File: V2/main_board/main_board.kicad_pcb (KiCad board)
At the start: 2 copper layers, 95 x 103.5 mm, 82 parts, among them J1 Conn_01x12, J2 Conn_01x12, J3 OUT_1, J4 OUT_2, J5 EXT_TEMP, J6 USB_C_Receptacle_USB2.0_16P, K1 EE2-3TNUH, Q1 BC817, Q2 BC817, SW1 SW_Slide_DPDT, SW2 SW_Push, SW3 SW_Push, U1 BQ24074RGT, U10 ESP32-S3-WROOM-2, U2 AP7361C-33E, U3 MAX17048G_T10, U4 EL817, U5 EL817, U6 PCF8563T, U8 DS18B20Z, U9 DS18B20Z, Y1 32.768khz

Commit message: In progress
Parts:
- removed C7, C8: 100uF, Capacitor_SMD:CP_Elec_8x10
- removed TP6: IO45, TestPoint:TestPoint_Pad_2.0x2.0mm
- removed TP7: IO46, TestPoint:TestPoint_Pad_2.0x2.0mm
- added K2: Relay_SPST_Latching_2coil, MH_switches:RELAY_G6CK-1117P-US_OMR, F.Cu at (63.0, 96.8)
- added Q3: BC817, Package_TO_SOT_SMD:SOT-23, F.Cu at (-7.70, 109.4)
- added Q4: BC817, Package_TO_SOT_SMD:SOT-23, F.Cu at (-13.5, 109.5)
- added R17: 0R, Resistor_SMD:R_0603_1608Metric, F.Cu at (231.8, 92.1)
- added R18: 120R, Resistor_SMD:R_0603_1608Metric, F.Cu at (-6.50, 94.2)
- added R19: 120R, Resistor_SMD:R_0603_1608Metric, F.Cu at (-14.8, 94.2)
- added U11: EL817, Package_DIP:SMDIP-4_W7.62mm, F.Cu at (-14.8, 101.0)
- added U7: EL817, Package_DIP:SMDIP-4_W7.62mm, F.Cu at (-6.50, 101.0)
- BT5: value RTC_BAT -> CR2032; footprint Battery:BatteryHolder_Keystone_1057_1x2032 -> Battery:BatteryHolder_Keystone_1058_1x2032
- D1: value GREEN -> M7; footprint LED_SMD:LED_0805_2012Metric -> Diode_SMD:D_SMA
- D2: value RED -> M7; footprint LED_SMD:LED_0805_2012Metric -> Diode_SMD:D_SMA
- F1: value 2A -> 10A; footprint Fuse:Fuse_Schurter_UMZ250 -> Fuse:Fuse_Schurter_UMT250; moved to B.Cu
- F2: value 2A -> 10A; footprint Fuse:Fuse_Schurter_UMZ250 -> Fuse:Fuse_Schurter_UMT250
- J1, J2: value Conn_01x12 -> Conn_01x14; footprint Connector_PinHeader_2.54mm:PinHeader_1x12_P2.54mm_Vertical_SMD_Pin1Left -> Connector_PinSocket_2.54mm:PinSocket_1x14_P2.54mm_Vertical_SMD_Pin1Left
- J3, J4: footprint TerminalBlock_Phoenix:TerminalBlock_Phoenix_MKDS-1,5-3_1x03_P5.00mm_Horizontal -> MH_connectors:SAMESKY_TBLH10-508-02BK
- K1: value EE2-3TNUH -> Relay_SPST_Latching_2coil; footprint Relay_SMD:Relay_DPDT_Kemet_EE2_NUH_DoubleCoil -> MH_switches:RELAY_G6CK-1117P-US_OMR
- R8, R9: value 1.5K -> 4.7k
- moved U2 136.7 mm to (-17.8, 71.0), turned to 90 degrees
- moved C4 129.8 mm to (-20.0, 77.5), turned to -90 degrees
- moved C5 126.9 mm to (-15.2, 77.5), turned to -90 degrees
- moved U5 117.2 mm to (-23.0, 101.1), turned to -90 degrees
- moved Q2 115.3 mm to (-24.2, 109.5), turned to -90 degrees
- moved Q1 115.3 mm to (-29.7, 109.5), turned to -90 degrees
- moved R11 114.2 mm to (-23.0, 94.3), turned to 0 degrees
- moved U4 111.7 mm to (-31.0, 101.1), turned to -90 degrees
- moved D6 110.0 mm to (217.5, 86.8), turned to 180 degrees
- moved R10 109.0 mm to (-31.2, 94.3), turned to 0 degrees
- moved BT5 107.6 mm to (221.2, 63.8)
- moved R12 106.6 mm to (220.5, 84.1), turned to 180 degrees
- moved C9 106.2 mm to (221.5, 92.3), turned to 180 degrees
- moved Y1 106.2 mm to (226.5, 92.3)
- moved J6 105.8 mm to (53.4, 69.6), turned to -90 degrees
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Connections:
- net /RELAY_RESET renamed /RELAY1_RESET
- net /RELAY_SET renamed /RELAY1_SET
- D1 pad 1: Net-(D1-K) -> +3V3
- D2 pad 1: Net-(D2-K) -> +3V3
- D5 pad 2: +3V3 -> Net-(D5-A)
- F1 pad 1: Net-(F1-Pad1) -> Net-(J3-Pin_1)
- F1 pad 2: Net-(J4-Pin_2) -> Net-(F1-Pad2)
- F2 pad 1: Net-(F2-Pad1) -> Net-(J4-Pin_1)
- F2 pad 2: Net-(J3-Pin_2) -> Net-(F2-Pad2)
- J1 pad 11: /LED_PWM -> GND
- J1 pad 12: GND -> /PGOOD
- R8 pad 1: VPP -> +3V3
- R8 pad 2: Net-(D1-K) -> /I2C_SDA
- R9 pad 1: Net-(D2-K) -> +3V3
- R9 pad 2: VPP -> /I2C_SCL
- U1 pad 7: Net-(D1-A) -> /PGOOD
- U1 pad 9: Net-(D2-A) -> /CHG
- U10 pad 16: Net-(U10-IO46) -> /RELAY2_RESET
- U10 pad 26: Net-(U10-IO45) -> /RELAY2_SET
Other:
- board size 95 x 103.5 mm -> 141.7 x 103.5 mm

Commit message: in progress
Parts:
- F1: moved to F.Cu
- moved K1 22.0 mm to (52.0, 141.2), turned to -90 degrees
- moved F1 18.3 mm to (67.2, 109.0)
- moved BT1 15.7 mm to (110.5, 69.2)
- moved SW1 15.1 mm to (153.8, 74.2)
- moved K2 11.7 mm to (51.6, 99.1), turned to -90 degrees
- moved J4 8.75 mm to (57.2, 121.8)
- moved BT4 8.49 mm to (110.8, 133.9)
- moved BT2 8.42 mm to (110.5, 90.6)
- moved BT3 7.96 mm to (110.6, 112.1)
- moved J3 7.29 mm to (57.2, 110.5)
- moved H2 6.67 mm to (145.5, 54.5)
- moved H4 6.67 mm to (145.5, 149.0), turned to 90 degrees
- moved F2 5.30 mm to (67.2, 121.8)
- moved H1 2.12 mm to (54.5, 54.5)
- moved H3 2.12 mm to (54.5, 149.0), turned to -90 degrees
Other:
- board size 141.7 x 103.5 mm -> 100 x 103.5 mm

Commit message: Push progress
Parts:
- removed J2: Conn_01x14, Connector_PinSocket_2.54mm:PinSocket_1x14_P2.54mm_Vertical_SMD_Pin1Left
- D1, D2, D3, D4: moved to B.Cu
- J1: value Conn_01x14 -> Conn_02x14_Top_Bottom; footprint Connector_PinSocket_2.54mm:PinSocket_1x14_P2.54mm_Vertical_SMD_Pin1Left -> Connector_PinHeader_2.54mm:PinHeader_2x14_P2.54mm_Vertical_SMD
- moved J5 147.4 mm to (51.2, 68.0), turned to -90 degrees
- moved R17 146.4 mm to (89.5, 57.5), turned to 90 degrees
- moved D5 144.2 mm to (89.5, 63.0), turned to 90 degrees
- moved Y1 136.3 mm to (94.8, 57.2), turned to 180 degrees
- moved TP3 136.1 mm to (92.8, 69.8), turned to 180 degrees
- moved U6 131.9 mm to (95.8, 63.0), turned to -90 degrees
- moved C9 126.7 mm to (99.8, 57.2), turned to 0 degrees
- moved R10 121.2 mm to (90.0, 98.5), turned to -90 degrees
- moved R12 121.2 mm to (100.8, 65.5), turned to 0 degrees
- moved D6 119.0 mm to (99.8, 69.5), turned to 0 degrees
- moved U4 114.5 mm to (83.5, 98.5), turned to 180 degrees
- moved R11 114.1 mm to (90.0, 110.5), turned to -90 degrees
- moved J6 112.1 mm to (131.7, 149.9), turned to 0 degrees
- moved C4 110.0 mm to (89.5, 87.9)
- moved C5 110.0 mm to (94.3, 87.8)
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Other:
- outline, holes or cut-outs redrawn

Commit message: Start layout
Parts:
- removed J4: OUT_2, MH_connectors:SAMESKY_TBLH10-508-02BK
- added J2: OUT_1, MH_connectors:CONN2_2604-1102_WAG, B.Cu at (60.5, 69.4)
- F1, F2: footprint Fuse:Fuse_Schurter_UMT250 -> Fuse:Fuseholder_Clip-5x20mm_Littelfuse_111_Lateral_P18.80x5.00mm_D1.17mm_Horizontal; moved to B.Cu
- J3: value OUT_1 -> OUT_2; footprint MH_connectors:SAMESKY_TBLH10-508-02BK -> MH_connectors:CONN2_2604-1102_WAG; moved to B.Cu
- moved C4 89.8 mm to (178.2, 74.0)
- moved C5 89.8 mm to (183.0, 74.0)
- moved U2 89.8 mm to (180.5, 67.5)
- moved J6 78.3 mm to (54.0, 140.0), turned to -90 degrees
- moved BT5 72.6 mm to (186.5, 32.5)
- moved C9 72.6 mm to (165.2, 26.0)
- moved D5 72.6 mm to (155.0, 31.8)
- moved D6 72.6 mm to (165.2, 38.2)
- moved R12 72.6 mm to (166.2, 34.2)
- moved R17 72.6 mm to (155.0, 26.2)
- moved TP3 72.6 mm to (158.2, 38.5)
- moved U6 72.6 mm to (161.2, 31.8)
- moved Y1 72.6 mm to (160.2, 26.0)
- moved R16 68.5 mm to (65.0, 141.0), turned to 0 degrees
- moved R15 65.5 mm to (65.0, 138.0), turned to 0 degrees
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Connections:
- F1 pad 1: Net-(J3-Pin_1) -> Net-(J2-Pin_2)
- F2 pad 1: Net-(J4-Pin_1) -> Net-(J3-Pin_2)
- K1 pad 14: Net-(J4-Pin_2) -> Net-(J3-Pin_1)
- K2 pad 14: Net-(J3-Pin_2) -> Net-(J2-Pin_1)
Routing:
- added copper zone on B.Cu, net Net-(F1-Pad2)
- added copper zone on F.Cu, net Net-(F1-Pad2)
- added copper zone on B.Cu, net Net-(F2-Pad2)
- added copper zone on F.Cu, net Net-(F2-Pad2)
- added copper zone on B.Cu, net Net-(J2-Pin_1)
- added copper zone on F.Cu, net Net-(J2-Pin_1)
- added copper zone on B.Cu, net Net-(J2-Pin_2)
- added copper zone on F.Cu, net Net-(J2-Pin_2)
- added copper zone on B.Cu, net Net-(J3-Pin_1)
- added copper zone on F.Cu, net Net-(J3-Pin_1)
- added copper zone on B.Cu, net Net-(J3-Pin_2)
- added copper zone on F.Cu, net Net-(J3-Pin_2)
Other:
- outline, holes or cut-outs redrawn

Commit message: Routing progress
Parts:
- H1, H2, H3, H4: footprint MountingHole:MountingHole_3.2mm_M3_ISO7380_Pad_TopBottom -> MountingHole:MountingHole_3.2mm_M3_ISO7380
- U11, U4, U5, U7: value EL817 -> LTV-217; footprint Package_DIP:SMDIP-4_W7.62mm -> Package_SO:SOP-4_4.4x2.6mm_P1.27mm
- moved TH1 90.8 mm to (134.4, 57.8), turned to 180 degrees
- moved C5 85.9 mm to (123.0, 135.5), turned to 180 degrees
- moved U2 83.0 mm to (129.5, 133.0), turned to 0 degrees
- moved Y1 81.2 mm to (118.0, 95.4), turned to -90 degrees
- moved C9 79.4 mm to (119.5, 90.9)
- moved C4 79.2 mm to (123.0, 130.8), turned to 180 degrees
- moved U6 74.5 mm to (123.8, 96.2), turned to 0 degrees
- moved BT5 73.3 mm to (124.2, 71.2), turned to 90 degrees
- moved R17 71.6 mm to (123.8, 90.7)
- moved R12 70.5 mm to (129.5, 94.4)
- moved D5 64.2 mm to (129.5, 90.7), turned to 180 degrees
- moved TP3 62.7 mm to (133.8, 96.2)
- moved D6 58.6 mm to (135.5, 88.8), turned to 90 degrees
- moved TP8 40.9 mm to (137.2, 126.5)
- moved R8 34.4 mm to (79.0, 141.8)
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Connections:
- J1 pad 10: /ADDR_LED -> /DISP_SCLK
- J1 pad 11: GND -> /BTN2
- J1 pad 12: /PGOOD -> /DISP_SDA
- J1 pad 13: /CHG -> /BTN3
- J1 pad 14: GND -> /ONEWIRE
- J1 pad 15: /DISP_BUSY -> /BTN4
- J1 pad 16: /DISP_RES -> /TS_INT
- J1 pad 17: /DISP_D/C -> /PRESENCE_RX
- J1 pad 18: /DISP_CS -> /TS_RST
- J1 pad 19: /DISP_SCLK -> /PRESENCE_TX
- J1 pad 2: +3V3 -> /DISP_BUSY
- J1 pad 20: /DISP_SDA -> unconnected-(J1-Pin_20-Pad20)
- J1 pad 21: /ONEWIRE -> /ADDR_LED
- J1 pad 22: /TS_INT -> GND
- J1 pad 23: /TS_RST -> GND
- J1 pad 24: /PRESENCE_TX -> /PGOOD
- J1 pad 25: /PRESENCE_RX -> /LED_PWM
- J1 pad 26: GND -> /CHG
- J1 pad 27: /LED_PWM -> GND
- J1 pad 3: /BTN1 -> +3V3
- J1 pad 4: /BTN2 -> /DISP_RES
- J1 pad 5: /BTN3 -> /I2C_SDA
- J1 pad 6: /BTN4 -> /DISP_D/C
- J1 pad 7: /SDA -> /I2C_SCL
- J1 pad 8: /SCL -> /DISP_CS
- J1 pad 9: /LED_G -> /BTN1
- U10 pad 16: /RELAY2_RESET -> unconnected-(U10-IO46-Pad16)
- U10 pad 22: /SCL -> unconnected-(U10-IO14-Pad22)
- U10 pad 23: /RTC_INT -> /RELAY1_SET
- U10 pad 24: /BTN3 -> /RELAY1_RESET
- U10 pad 25: /BTN4 -> /RELAY2_RESET
- U10 pad 32: /LED_G -> /BTN4
- U10 pad 33: /LED_PWM -> /BTN3
- U10 pad 34: /BTN1 -> /BTN2
- U10 pad 35: /BTN2 -> /BTN1
- U10 pad 5: /RELAY1_SET -> /RTC_INT
- U10 pad 6: /RELAY1_RESET -> unconnected-(U10-IO6-Pad6)
- U10 pad 8: /SDA -> unconnected-(U10-IO15-Pad8)
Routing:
- net /ONEWIRE: track 0.00 -> 139.1 mm, vias 0 -> 5
- net +BATT: track 0.00 -> 117.9 mm
- net /I2C_SDA: track 0.00 -> 84.6 mm, vias 0 -> 2
- net /I2C_SCL: track 0.00 -> 77.6 mm, vias 0 -> 2
- net /D+: track 0.00 -> 68.5 mm, vias 0 -> 4
- net /D-: track 0.00 -> 67.4 mm, vias 0 -> 2
- net /BTN1: track 0.00 -> 61.5 mm, vias 0 -> 2
- net /BTN2: track 0.00 -> 56.8 mm, vias 0 -> 2
- net /PRESENCE_RX: track 0.00 -> 55.7 mm, vias 0 -> 2
- net /PRESENCE_TX: track 0.00 -> 53.8 mm, vias 0 -> 2
- net /RELAY1_SET: track 0.00 -> 52.9 mm
- net /BTN3: track 0.00 -> 51.2 mm, vias 0 -> 2
- net /BTN4: track 0.00 -> 46.5 mm, vias 0 -> 2
- net /RELAY1_RESET: track 0.00 -> 43.6 mm
- net /VBUS_SW: track 0.00 -> 29.6 mm
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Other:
- outline, holes or cut-outs redrawn
- copper layers 2 -> 4

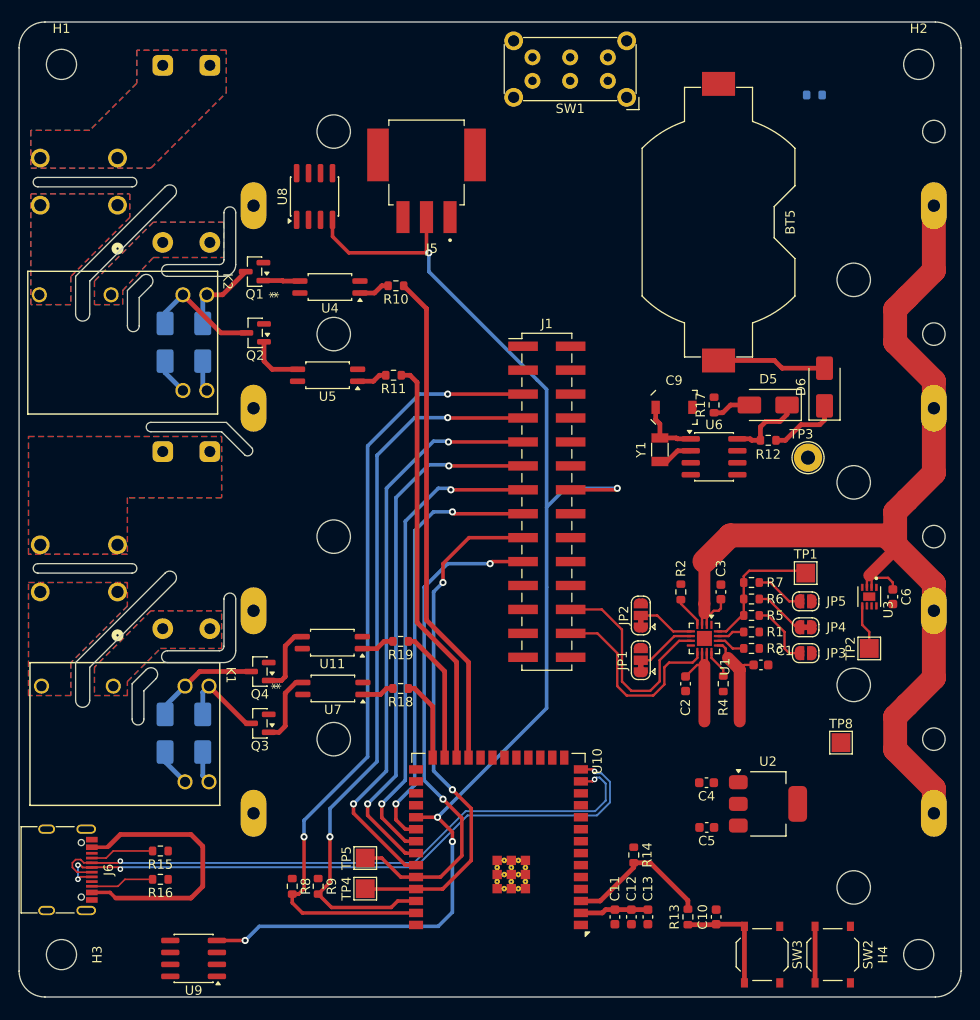
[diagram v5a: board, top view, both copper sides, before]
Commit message: Schematic updates
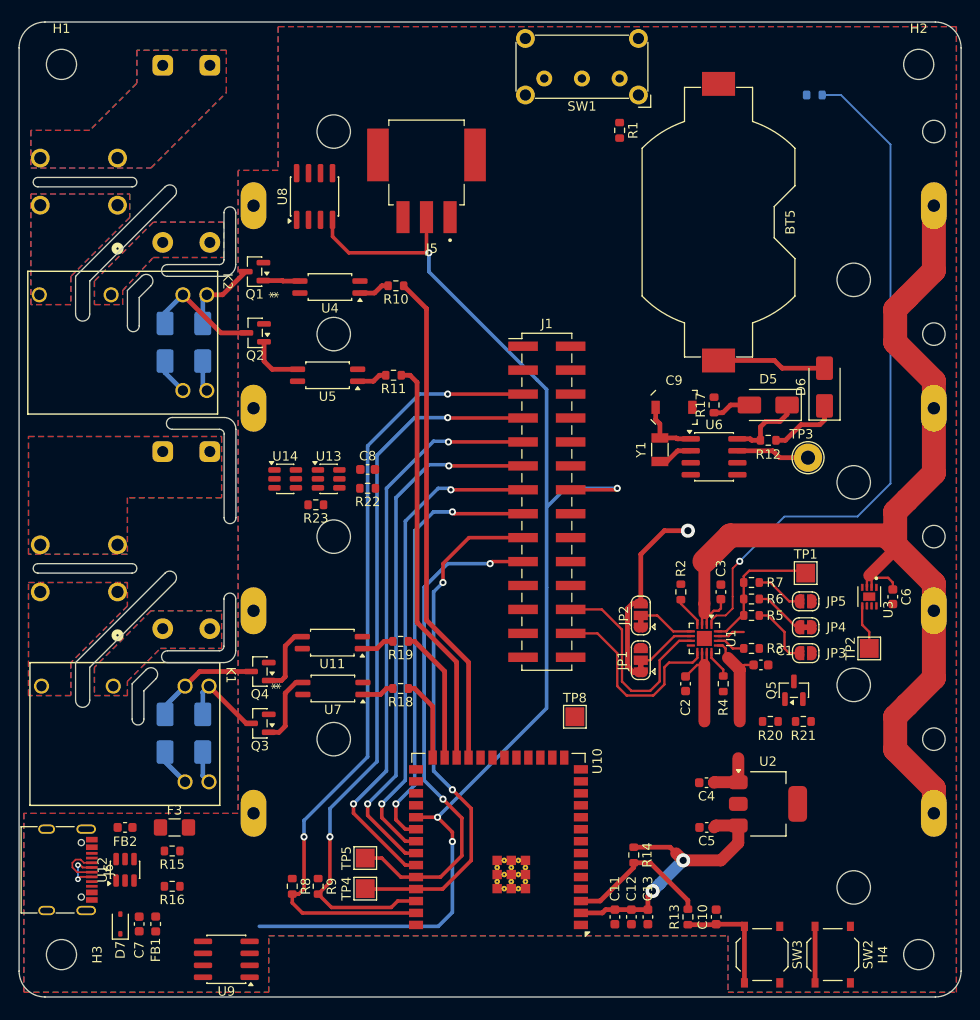
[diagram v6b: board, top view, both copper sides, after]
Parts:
- added C7: 100nF, Capacitor_SMD:C_0603_1608Metric, F.Cu at (62.8, 145.8)
- added C8: 100nF, Capacitor_SMD:C_0603_1608Metric, F.Cu at (87.0, 97.5)
- added D7: D_TVS, Diode_SMD:D_SOD-323, F.Cu at (60.8, 145.8)
- added F3: 750mA, Fuse:Fuse_1206_3216Metric_Pad1.42x1.75mm_HandSolder, F.Cu at (66.5, 135.5)
- added FB1: FerriteBead_Small, Inductor_SMD:L_0603_1608Metric, F.Cu at (64.5, 145.8)
- added FB2: FerriteBead_Small, Inductor_SMD:L_0603_1608Metric, F.Cu at (61.2, 135.5)
- added Q5: 2N7002, Package_TO_SOT_SMD:SOT-23, F.Cu at (132.2, 120.9)
- added R20: 100R, Resistor_SMD:R_0603_1608Metric, F.Cu at (129.8, 124.2)
- added R21: 10k, Resistor_SMD:R_0603_1608Metric, F.Cu at (133.2, 124.2)
- added R22: 100R, Resistor_SMD:R_0603_1608Metric, F.Cu at (87.0, 99.5)
- added R23: 1K, Resistor_SMD:R_0603_1608Metric, F.Cu at (81.5, 101.2)
- added U12: SRV05-4, Package_TO_SOT_SMD:SOT-23-6, F.Cu at (61.2, 140.0)
- added U13: DW01A, Package_TO_SOT_SMD:SOT-23-6, F.Cu at (82.9, 98.5)
- added U14: FS8205A, Package_TO_SOT_SMD:SOT-23-6, F.Cu at (78.2, 98.5)
- R1: value 10K -> 100k
- SW1: value SW_Slide_DPDT -> SW_SPDT; footprint Button_Switch_THT:SW_E-Switch_EG2219_DPDT_Angled -> Button_Switch_THT:SW_E-Switch_EG1224_SPDT_Angled
- U1: value BQ24074RGT -> BQ24075RGT
- moved R1 55.1 mm to (113.8, 61.5), turned to -90 degrees
- moved TP8 28.4 mm to (109.0, 123.8)
- moved U9 3.48 mm to (72.0, 149.5)
- moved R16 1.45 mm to (66.2, 141.8)
- moved SW1 1.27 mm to (113.8, 56.0)
- moved R15 1.25 mm to (66.2, 138.0)
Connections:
- BT1 pad 2: GND -> -BATT
- BT2 pad 2: GND -> -BATT
- BT3 pad 2: GND -> -BATT
- BT4 pad 2: GND -> -BATT
- C1 pad 1: VBUS -> +5V
- C2 pad 2: /VPP_SW -> VPP
- J6 pad A1: GND -> Earth
- J6 pad A12: GND -> Earth
- J6 pad A4: /VBUS_SW -> VBUS
- J6 pad A9: /VBUS_SW -> VBUS
- J6 pad B1: GND -> Earth
- J6 pad B12: GND -> Earth
- J6 pad B4: /VBUS_SW -> VBUS
- J6 pad B9: /VBUS_SW -> VBUS
- J6 pad S1: GND -> Earth
- R1 pad 1: Net-(U1-ITERM) -> Net-(SW1-A)
- R1 pad 2: GND -> +BATT
- SW1 pad 1: unconnected-(SW1-A-Pad1) -> Net-(SW1-A)
- SW1 pad 2: VPP -> /SYSOFF
- SW1 pad 3: /VPP_SW -> GND
- U1 pad 10: /VPP_SW -> VPP
- U1 pad 11: /VPP_SW -> VPP
- U1 pad 13: VBUS -> +5V
- U1 pad 15: Net-(U1-ITERM) -> /SYSOFF
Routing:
- net Net-(U1-TS): track 0.00 -> 73.4 mm, vias 0 -> 1
- net /D+: track 68.5 -> 4.69 mm, vias 4 -> 2
- net /D-: track 67.4 -> 5.14 mm, vias 2 -> 0
- net VPP: track 0.00 -> 37.3 mm, vias 0 -> 1
- net /VBUS_SW: track 29.6 -> 0.00 mm
- net +3V3: track 21.9 -> 45.7 mm, vias 0 -> 2
- net /VPP_SW: track 11.5 -> 0.00 mm
- net VBUS: track 11.0 -> 0.00 mm
- net +5V: track 0.00 -> 11.0 mm
- net Net-(U6-CLKO): track 0.00 -> 7.80 mm
- net /CC1: track 6.76 -> 0.00 mm
- net /CC2: track 6.76 -> 0.00 mm
- net /ONEWIRE: track 139.1 -> 134.0 mm, vias 5 -> 4
- net Net-(U1-ITERM): track 2.92 -> 0.00 mm
- net /SYSOFF: track 0.00 -> 2.92 mm
- added copper zone on B.Cu, net GND
- added copper zone on F.Cu, net GND
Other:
- outline, holes or cut-outs redrawn
- copper layers 4 -> 2

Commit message: main board in good spot
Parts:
- removed the JP3 at (133.5, 117.0)
- removed the R2 at (120.2, 110.5)
- removed the R5 at (127.8, 113.0)
- removed the R6 at (127.8, 111.2)
- removed the R7 at (127.8, 109.5)
- added R1: 47k, Resistor_SMD:R_0603_1608Metric, F.Cu at (120.2, 110.5)
- added R8: 3.9k, Resistor_SMD:R_0603_1608Metric, F.Cu at (127.8, 112.5)
- added R9: 910R, Resistor_SMD:R_0603_1608Metric, F.Cu at (127.8, 110.7)
- added REF**: KiCad-Logo2_6mm_SilkScreen, Symbol:KiCad-Logo2_6mm_SilkScreen, F.Cu at (135.5, 54.2)
- added REF**: OSHW-Logo2_9.8x8mm_SilkScreen, Symbol:OSHW-Logo2_9.8x8mm_SilkScreen, F.Cu at (82.5, 55.2)
- added TP2: IO3, TestPoint:TestPoint_Pad_2.0x2.0mm, F.Cu at (118.0, 140.5)
- added TP3: IO3, TestPoint:TestPoint_Pad_2.0x2.0mm, F.Cu at (114.8, 140.5)
- added TP5: IO3, TestPoint:TestPoint_Pad_2.0x2.0mm, F.Cu at (105.5, 122.0)
- F1: renamed from F3; value 750mA -> 2A
- JP3: renamed from JP4; value 1A -> 230mA
- JP4: renamed from JP5; value 0.5A -> 930mA
- SW3: renamed from SW1; moved to B.Cu
- moved R6 8.20 mm to (122.5, 142.2), turned to 180 degrees
- moved R17 8.00 mm to (105.8, 61.2)
- moved SW3 8.00 mm to (105.8, 56.0), turned to 0 degrees
- moved TP1 2.50 mm to (131.0, 108.5)
- moved TP4 1.77 mm to (109.2, 122.0)
- moved JP3 1.20 mm to (133.5, 115.5)
- moved JP4 1.20 mm to (133.5, 112.7)
- moved R13 0.25 mm to (81.8, 101.2)
- turned H1 to 180 degrees
- turned H2 to 180 degrees
- turned H4 to 0 degrees
- turned TP9 to -90 degrees
- turned U1 to -90 degrees
- renumbered C10 to C1, C9 to C10, C4 to C11, C5 to C12, C6 to C13, C7 to C2, C11 to C3, C12 to C4, C8 to C5, C13 to C6, C1 to C7, C2 to C8, C3 to C9, D7 to D1, D3 to D2, D4 to D3, D5 to D4, D6 to D5, D1 to D6, D2 to D7, F1 to F2, F2 to F3, J6 to J1, J1 to J3, J3 to J4, K2 to K1, K1 to K2, Q5 to Q1, Q1 to Q2, Q2 to Q3, Q3 to Q4, Q4 to Q5, R22 to R10, R9 to R11, R8 to R12, R23 to R13, R20 to R14, R21 to R15, R10 to R16, R1 to R17, R11 to R18, R17 to R19, R3 to R2, R12 to R20, R18 to R21, R19 to R22, R13 to R3, R15 to R4, R4 to R5, R14 to R6, R16 to R7, SW2 to SW1, SW3 to SW2, TP8 to TP4, TP5 to TP6, TP4 to TP7, TP3 to TP8, TP2 to TP9, U12 to U1, U3 to U10, U7 to U11, U8 to U12, U9 to U13, U11 to U14, U1 to U2, U13 to U3, U10 to U4, U14 to U5, U4 to U6, U2 to U7, U6 to U8, U5 to U9
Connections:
- J3 pad 20: unconnected-(J1-Pin_20-Pad20) -> /ALS_INT
- J3 pad 22: GND -> /LED_G
- U4 pad 10: /TS_RST -> /TS_INT
- U4 pad 11: /ALS_INT -> /DISP_RES
- U4 pad 12: /DISP_RES -> /DISP_BUSY
- U4 pad 16: unconnected-(U10-IO46-Pad16) -> Net-(U4-IO46)
- U4 pad 21: /SPI_MISO -> /LED_PWM
- U4 pad 22: unconnected-(U10-IO14-Pad22) -> /ADDR_LED
- U4 pad 4: /ADDR_LED -> Net-(U4-IO4)
- U4 pad 6: unconnected-(U10-IO6-Pad6) -> Net-(U4-IO6)
- U4 pad 7: /DISP_BUSY -> /LED_G
- U4 pad 8: unconnected-(U10-IO15-Pad8) -> /ALS_INT
- U4 pad 9: /TS_INT -> /TS_RST
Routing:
- net +3V3: track 45.7 -> 359.5 mm, vias 2 -> 7
- net /SYSOFF: track 2.92 -> 108.6 mm, vias 0 -> 2
- net +BATT: track 117.9 -> 220.5 mm, vias 0 -> 3
- net +5V: track 11.0 -> 104.2 mm, vias 0 -> 4
- net VPP: track 37.3 -> 115.0 mm, vias 1 -> 3
- net /I2C_SDA: track 84.6 -> 160.7 mm, vias 2 -> 6
- net /I2C_SCL: track 77.6 -> 151.2 mm, vias 2 -> 4
- net -BATT: track 0.00 -> 72.6 mm
- net /D+: track 4.69 -> 71.4 mm, vias 2 -> 4
- net /D-: track 5.14 -> 70.3 mm, vias 0 -> 2
- net /DISP_BUSY: track 0.00 -> 58.0 mm, vias 0 -> 2
- net /DISP_RES: track 0.00 -> 56.4 mm, vias 0 -> 2
- net /BOOT0: track 6.00 -> 61.7 mm, vias 0 -> 2
- net /RTC_INT: track 0.00 -> 51.0 mm, vias 0 -> 2
- net /DISP_D/C: track 0.00 -> 50.6 mm, vias 0 -> 2
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- added copper zone on B.Cu, net Earth
- added copper zone on F.Cu, net Earth
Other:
- board text added: "BOOT"
- board text added: "GND ONEWIRE +3V3"
- board text added: "HSTAT V2 Main Board"
- board text added: "JLCJLCJLCJLC"
- board text added: "McKay Humpherys Brian Humpherys"
- board text added: "OFF"
- board text added: "ON"
- board text added: "RESET"

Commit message: Display board in good spot
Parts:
- added C14: 100nF, Capacitor_SMD:C_0603_1608Metric, F.Cu at (72.0, 146.0)
- added C15: 100nF, Capacitor_SMD:C_0603_1608Metric, F.Cu at (85.0, 68.5)
- J3: footprint Connector_PinHeader_2.54mm:PinHeader_2x14_P2.54mm_Vertical_SMD -> Connector_PinSocket_2.54mm:PinSocket_2x14_P2.54mm_Vertical_SMD
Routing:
- net +3V3: track 359.5 -> 362.6 mm
